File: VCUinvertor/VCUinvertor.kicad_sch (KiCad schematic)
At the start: 106 parts, among them J7 PowerSupply, J9 BRAKE LIGHT, Q1 2N7002, Q10 2N7002, Q11 BC848C, Q12 BCP51, Q2 2N7002, Q3 2N7002, Q4 2N7002, Q5 2N7002, Q6 2N7002, Q7 2N7002, Q8 2N7002, Q9 2N7002, U1 TJA1448ATK, U2 REF3433T, U3 TLV76150DCY

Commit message: SMD components resized for Handsoldering (0805 -> 1206)
*Resistors & Capacitors are now upgraded to size 1206 for easy handsoldering
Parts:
- C1, C10, C11, C12, C2, C3, C4, C5, C6, C7, C8, C9: footprint Capacitor_SMD:C_0805_2012Metric_Pad1.18x1.45mm_HandSolder -> Capacitor_SMD:C_1206_3216Metric_Pad1.33x1.80mm_HandSolder
- R1, R10, R11, R12, R13, R14, R15, R16, R17, R18, R19, R2, R20, R21, R22, R23, R24, R25, R26, R3, R4, R5, R6, R63, R64, R7, R8, R9: footprint Resistor_SMD:R_0805_2012Metric -> Resistor_SMD:R_1206_3216Metric_Pad1.30x1.75mm_HandSolder
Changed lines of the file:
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@@
 			)
 		)
-		(property "Footprint" "Resistor_SMD:R_0805_2012Metric"
+		(property "Footprint" "Resistor_SMD:R_1206_3216Metric_Pad1.30x1.75mm_HandSolder"
 			(at 264.16 255.27 0)
 			(effects
@@
 			)
 		)
-		(property "Footprint" "Resistor_SMD:R_0805_2012Metric"
+		(property "Footprint" "Resistor_SMD:R_1206_3216Metric_Pad1.30x1.75mm_HandSolder"
 			(at 257.81 184.15 0)
 			(effects
@@
 			)
 		)
-		(property "Footprint" "Resistor_SMD:R_0805_2012Metric"
+		(property "Footprint" "Resistor_SMD:R_1206_3216Metric_Pad1.30x1.75mm_HandSolder"
 			(at 196.85 264.16 0)
 			(effects
@@
 			)
 		)
-		(property "Footprint" "Resistor_SMD:R_0805_2012Metric"
+		(property "Footprint" "Resistor_SMD:R_1206_3216Metric_Pad1.30x1.75mm_HandSolder"
 			(at 204.47 226.06 0)
 			(effects
@@
 			)
 		)
-		(property "Footprint" "Capacitor_SMD:C_0805_2012Metric_Pad1.18x1.45mm_HandSolder"
+		(property "Footprint" "Capacitor_SMD:C_1206_3216Metric_Pad1.33x1.80mm_HandSolder"
 			(at 339.09 158.75 0)
 			(effects
@@
 			)
 		)
-		(property "Footprint" "Capacitor_SMD:C_0805_2012Metric_Pad1.18x1.45mm_HandSolder"
+		(property "Footprint" "Capacitor_SMD:C_1206_3216Metric_Pad1.33x1.80mm_HandSolder"
 			(at 236.22 55.88 0)
 			(effects
@@
 			)
 		)
-		(property "Footprint" "Resistor_SMD:R_0805_2012Metric"
+		(property "Footprint" "Resistor_SMD:R_1206_3216Metric_Pad1.30x1.75mm_HandSolder"
 			(at 196.85 234.95 0)
 			(effects
@@
 			)
 		)
-		(property "Footprint" "Resistor_SMD:R_0805_2012Metric"
+		(property "Footprint" "Resistor_SMD:R_1206_3216Metric_Pad1.30x1.75mm_HandSolder"
 			(at 322.58 238.76 0)
 			(effects
@@
 			)
 		)
-		(property "Footprint" "Resistor_SMD:R_0805_2012Metric"
+		(property "Footprint" "Resistor_SMD:R_1206_3216Metric_Pad1.30x1.75mm_HandSolder"
 			(at 204.47 175.26 0)
 			(effects
@@
 			)
 		)
-		(property "Footprint" "Resistor_SMD:R_0805_2012Metric"
+		(property "Footprint" "Resistor_SMD:R_1206_3216Metric_Pad1.30x1.75mm_HandSolder"
 			(at 204.47 200.66 0)
 			(effects
@@
 			)
 		)
-		(property "Footprint" "Resistor_SMD:R_0805_2012Metric"
+		(property "Footprint" "Resistor_SMD:R_1206_3216Metric_Pad1.30x1.75mm_HandSolder"
 			(at 365.76 232.41 0)
 			(effects
@@
 			)
 		)
-		(property "Footprint" "Resistor_SMD:R_0805_2012Metric"
+		(property "Footprint" "Resistor_SMD:R_1206_3216Metric_Pad1.30x1.75mm_HandSolder"
 			(at 196.85 158.75 0)
 			(effects
@@
 			)
 		)
-		(property "Footprint" "Resistor_SMD:R_0805_2012Metric"
+		(property "Footprint" "Resistor_SMD:R_1206_3216Metric_Pad1.30x1.75mm_HandSolder"
 			(at 196.85 184.15 0)
 			(effects
@@
 			)
 		)
-		(property "Footprint" "Resistor_SMD:R_0805_2012Metric"
+		(property "Footprint" "Resistor_SMD:R_1206_3216Metric_Pad1.30x1.75mm_HandSolder"
 			(at 257.81 209.55 0)
 			(effects
@@
 			)
 		)
-		(property "Footprint" "Resistor_SMD:R_0805_2012Metric"
+		(property "Footprint" "Resistor_SMD:R_1206_3216Metric_Pad1.30x1.75mm_HandSolder"
 			(at 265.43 175.26 0)
 			(effects
@@
 			)
 		)
-		(property "Footprint" "Resistor_SMD:R_0805_2012Metric"
+		(property "Footprint" "Resistor_SMD:R_1206_3216Metric_Pad1.30x1.75mm_HandSolder"
 			(at 257.81 234.95 0)
 			(effects
@@
 			)
 		)
-		(property "Footprint" "Capacitor_SMD:C_0805_2012Metric_Pad1.18x1.45mm_HandSolder"
+		(property "Footprint" "Capacitor_SMD:C_1206_3216Metric_Pad1.33x1.80mm_HandSolder"
 			(at 308.61 81.28 0)
 			(effects
@@
 			)
 		)
-		(property "Footprint" "Resistor_SMD:R_0805_2012Metric"
+		(property "Footprint" "Resistor_SMD:R_1206_3216Metric_Pad1.30x1.75mm_HandSolder"
 			(at 203.2 92.71 0)
 			(effects
@@
 			)
 		)
-		(property "Footprint" "Resistor_SMD:R_0805_2012Metric"
+		(property "Footprint" "Resistor_SMD:R_1206_3216Metric_Pad1.30x1.75mm_HandSolder"
 			(at 264.16 149.86 0)
 			(effects
@@
 			)
 		)
-		(property "Footprint" "Resistor_SMD:R_0805_2012Metric"
+		(property "Footprint" "Resistor_SMD:R_1206_3216Metric_Pad1.30x1.75mm_HandSolder"
 			(at 196.85 209.55 0)
 			(effects
@@
 			)
 		)
-		(property "Footprint" "Resistor_SMD:R_0805_2012Metric"
+		(property "Footprint" "Resistor_SMD:R_1206_3216Metric_Pad1.30x1.75mm_HandSolder"
 			(at 256.54 264.16 0)
 			(effects
@@
 			)
 		)
-		(property "Footprint" "Capacitor_SMD:C_0805_2012Metric_Pad1.18x1.45mm_HandSolder"
+		(property "Footprint" "Capacitor_SMD:C_1206_3216Metric_Pad1.33x1.80mm_HandSolder"
 			(at 361.95 82.55 0)
 			(effects
@@
 			)
 		)
-		(property "Footprint" "Resistor_SMD:R_0805_2012Metric"
+		(property "Footprint" "Resistor_SMD:R_1206_3216Metric_Pad1.30x1.75mm_HandSolder"
 			(at 322.58 229.87 0)
 			(effects
@@
 			)
 		)
-		(property "Footprint" "Resistor_SMD:R_0805_2012Metric"
+		(property "Footprint" "Resistor_SMD:R_1206_3216Metric_Pad1.30x1.75mm_HandSolder"
 			(at 201.93 76.2 0)
 			(effects
@@
 			)
 		)
-		(property "Footprint" "Capacitor_SMD:C_0805_2012Metric_Pad1.18x1.45mm_HandSolder"
+		(property "Footprint" "Capacitor_SMD:C_1206_3216Metric_Pad1.33x1.80mm_HandSolder"
 			(at 218.44 55.88 0)
 			(effects
@@
 			)
 		)
-		(property "Footprint" "Capacitor_SMD:C_0805_2012Metric_Pad1.18x1.45mm_HandSolder"
+		(property "Footprint" "Capacitor_SMD:C_1206_3216Metric_Pad1.33x1.80mm_HandSolder"
 			(at 318.77 158.75 0)
 			(effects
@@
 			)
 		)
-		(property "Footprint" "Resistor_SMD:R_0805_2012Metric"
+		(property "Footprint" "Resistor_SMD:R_1206_3216Metric_Pad1.30x1.75mm_HandSolder"
 			(at 203.2 86.36 0)
 			(effects
@@
 			)
 		)
-		(property "Footprint" "Capacitor_SMD:C_0805_2012Metric_Pad1.18x1.45mm_HandSolder"
+		(property "Footprint" "Capacitor_SMD:C_1206_3216Metric_Pad1.33x1.80mm_HandSolder"
 			(at 369.57 82.55 0)
 			(effects
@@
 			)
 		)
-		(property "Footprint" "Capacitor_SMD:C_0805_2012Metric_Pad1.18x1.45mm_HandSolder"
+		(property "Footprint" "Capacitor_SMD:C_1206_3216Metric_Pad1.33x1.80mm_HandSolder"
 			(at 213.36 55.88 0)
 			(effects
@@
 			)
 		)
-		(property "Footprint" "Capacitor_SMD:C_0805_2012Metric_Pad1.18x1.45mm_HandSolder"
+		(property "Footprint" "Capacitor_SMD:C_1206_3216Metric_Pad1.33x1.80mm_HandSolder"
 			(at 196.85 90.17 0)
 			(effects
@@
 			)
 		)
-		(property "Footprint" "Resistor_SMD:R_0805_2012Metric"
+		(property "Footprint" "Resistor_SMD:R_1206_3216Metric_Pad1.30x1.75mm_HandSolder"
 			(at 256.54 158.75 0)
 			(effects
@@
 			)
 		)
-		(property "Footprint" "Resistor_SMD:R_0805_2012Metric"
+		(property "Footprint" "Resistor_SMD:R_1206_3216Metric_Pad1.30x1.75mm_HandSolder"
 			(at 201.93 69.85 0)
 			(effects
@@
 			)
 		)
-		(property "Footprint" "Capacitor_SMD:C_0805_2012Metric_Pad1.18x1.45mm_HandSolder"
+		(property "Footprint" "Capacitor_SMD:C_1206_3216Metric_Pad1.33x1.80mm_HandSolder"
 			(at 361.95 156.21 0)
 			(effects
@@
 			)
 		)
-		(property "Footprint" "Capacitor_SMD:C_0805_2012Metric_Pad1.18x1.45mm_HandSolder"
+		(property "Footprint" "Capacitor_SMD:C_1206_3216Metric_Pad1.33x1.80mm_HandSolder"
 			(at 196.85 72.39 0)
 			(effects
@@
 			)
 		)
-		(property "Footprint" "Resistor_SMD:R_0805_2012Metric"
+		(property "Footprint" "Resistor_SMD:R_1206_3216Metric_Pad1.30x1.75mm_HandSolder"
 			(at 265.43 200.66 0)
 			(effects
@@
 			)
 		)
-		(property "Footprint" "Capacitor_SMD:C_0805_2012Metric_Pad1.18x1.45mm_HandSolder"
+		(property "Footprint" "Capacitor_SMD:C_1206_3216Metric_Pad1.33x1.80mm_HandSolder"
 			(at 387.35 157.48 0)
 			(effects
@@
 			)
 		)
-		(property "Footprint" "Resistor_SMD:R_0805_2012Metric"
+		(property "Footprint" "Resistor_SMD:R_1206_3216Metric_Pad1.30x1.75mm_HandSolder"
 			(at 204.47 149.86 0)
 			(effects
@@
 			)
 		)
-		(property "Footprint" "Resistor_SMD:R_0805_2012Metric"
+		(property "Footprint" "Resistor_SMD:R_1206_3216Metric_Pad1.30x1.75mm_HandSolder"
 			(at 383.54 224.79 0)
 			(effects
@@
 			)
 		)
-		(property "Footprint" "Resistor_SMD:R_0805_2012Metric"
+		(property "Footprint" "Resistor_SMD:R_1206_3216Metric_Pad1.30x1.75mm_HandSolder"
 			(at 204.47 255.27 0)
 			(effects
@@
 			)
 		)
-		(property "Footprint" "Resistor_SMD:R_0805_2012Metric"
+		(property "Footprint" "Resistor_SMD:R_1206_3216Metric_Pad1.30x1.75mm_HandSolder"
 			(at 265.43 226.06 0)
 			(effects

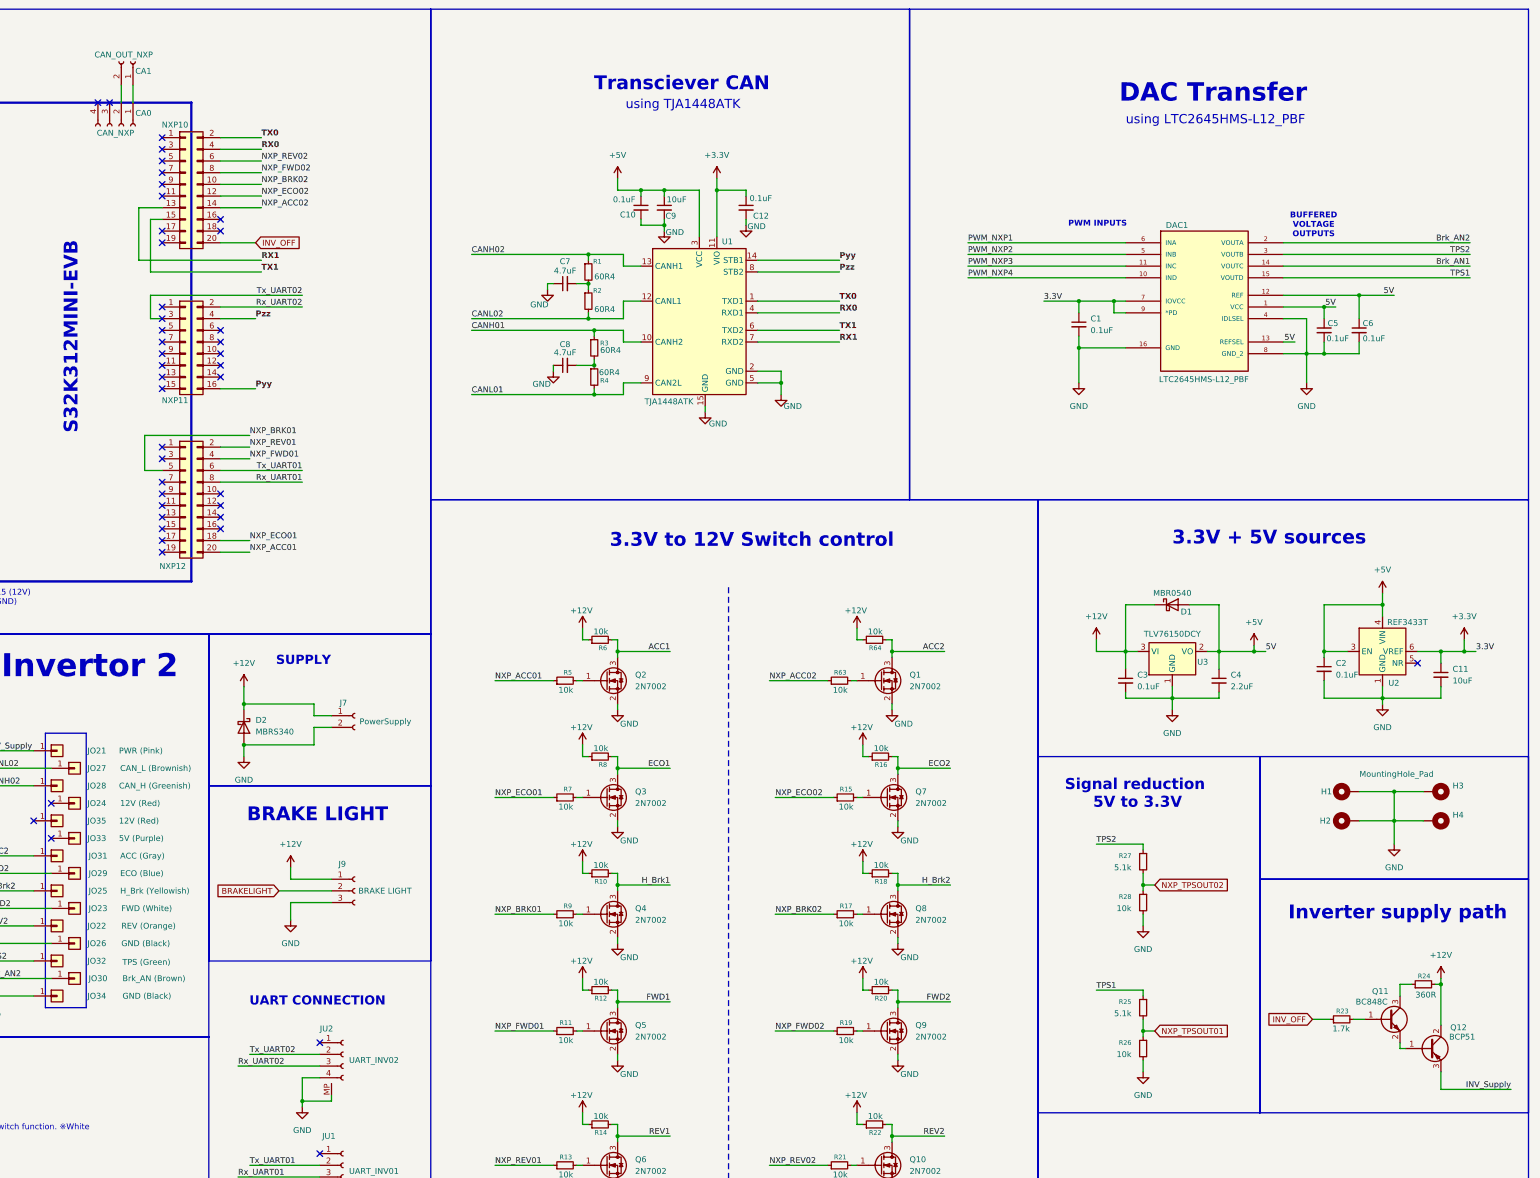
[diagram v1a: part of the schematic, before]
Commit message: TestPoints added
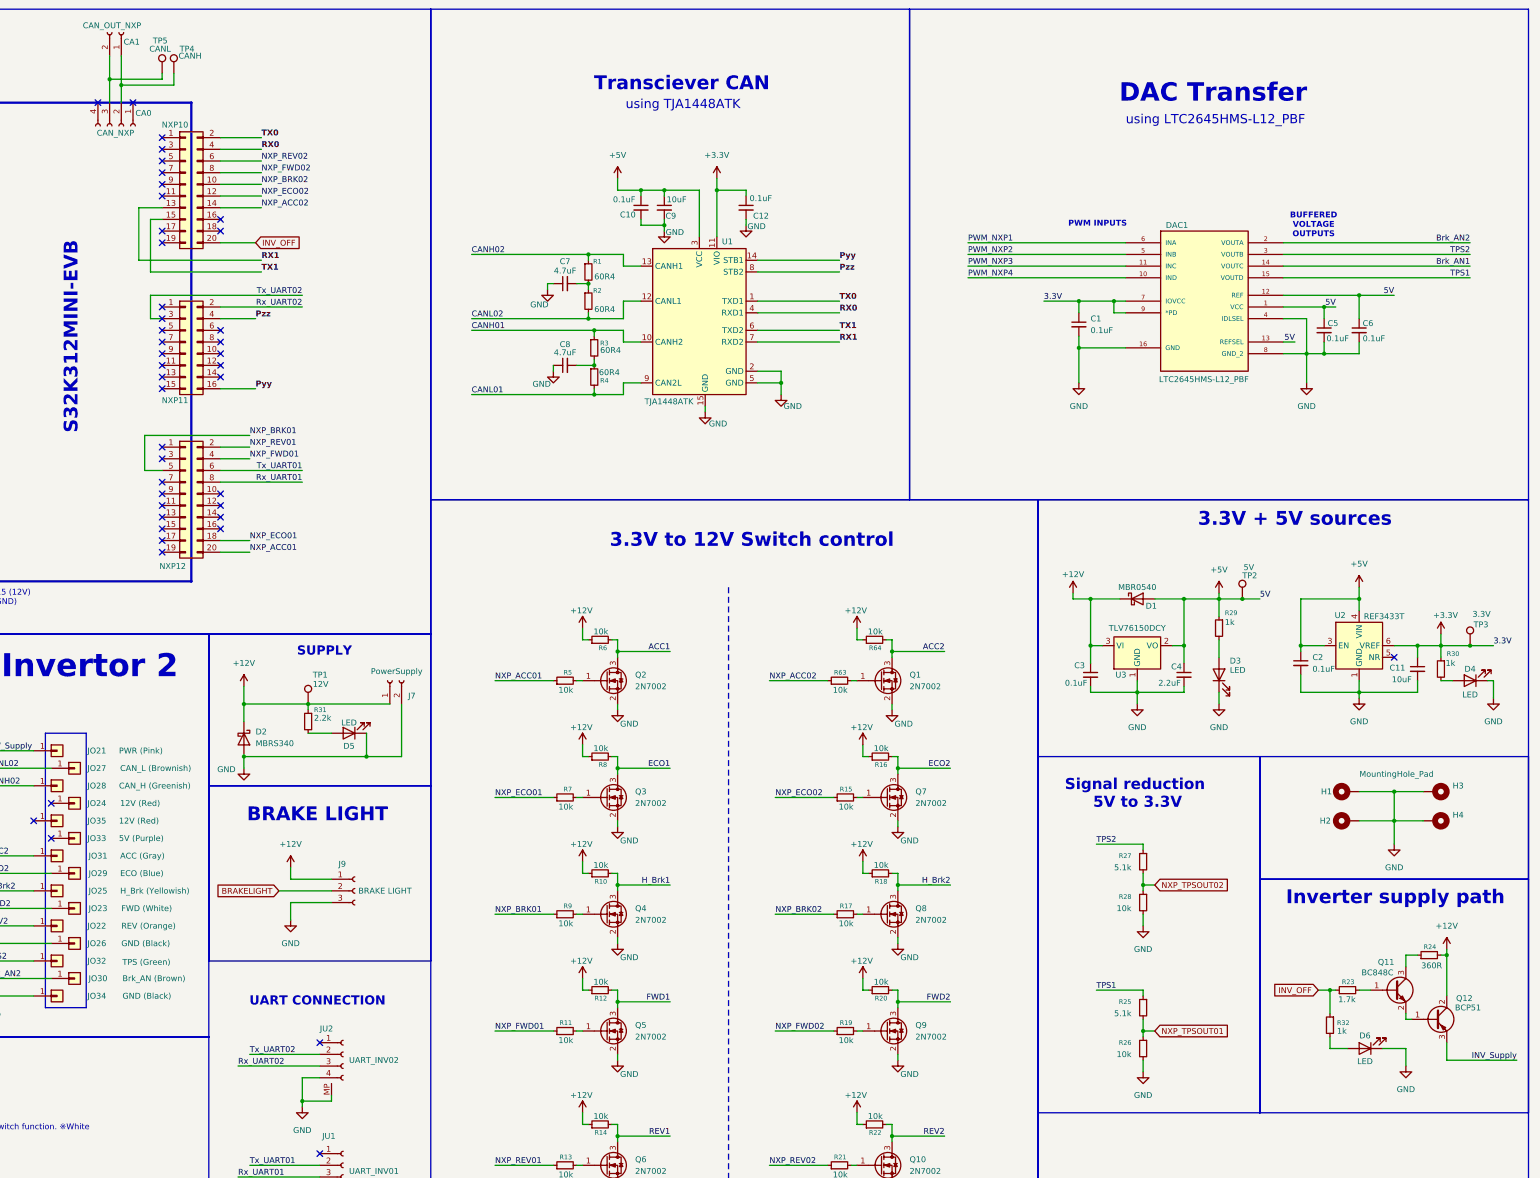
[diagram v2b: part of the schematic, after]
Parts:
- added D3, D4, D5, D6: LED, LED_SMD:LED_0805_2012Metric_Pad1.15x1.40mm_HandSolder, symbol Device:LED
- added R29, R30, R32: 1k, Resistor_SMD:R_0805_2012Metric, symbol Device:R_Small
- added R31: 2.2k, Resistor_SMD:R_0805_2012Metric, symbol Device:R_Small
- added TP1: 12V, TestPoint:TestPoint_Pad_D1.5mm, symbol Connector:TestPoint
- added TP2: 5V, TestPoint:TestPoint_Pad_D1.5mm, symbol Connector:TestPoint
- added TP3: 3.3V, TestPoint:TestPoint_Pad_D1.5mm, symbol Connector:TestPoint
- added TP4: CANH, TestPoint:TestPoint_Pad_D1.5mm, symbol Connector:TestPoint
- added TP5: CANL, TestPoint:TestPoint_Pad_D1.5mm, symbol Connector:TestPoint
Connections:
- net +12V: now also R31.1, TP1.1
- net +3.3V: now also R30.1, TP3.1
- net +5V: now also R29.1, TP2.1
- net GND: now also D3.1 (K), D4.1 (K), D5.1 (K), D6.1 (K)
- net INV_OFF: now also R32.1
- net at CA1.1 (Pin_1): now also CA0.2 (Pin_2), TP4.1; no longer CA0.1 (Pin_1)
- net at CA1.2 (Pin_2): now also CA0.3 (Pin_3), TP5.1; no longer CA0.2 (Pin_2)
- new net: D6.2 (A), R32.2
- new net: D5.2 (A), R31.2
- new net: D3.2 (A), R29.2
- new net: D4.2 (A), R30.2
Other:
- moved on the sheet: C11, C2, C3, C4, CA1, D1, D2, J7, Q11, Q12, R23, R24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
